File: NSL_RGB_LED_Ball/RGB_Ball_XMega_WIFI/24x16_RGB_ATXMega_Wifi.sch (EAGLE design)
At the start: 102 parts, among them IC2 TLC5947XLP, IC3 TLC5947XLP, IC4 TLC5947XLP, IC5 MCP73123, IC6 CC3000, IC7 MMA7455L, IC8 OPA344, X1 NX3225GA XC1972CT-ND

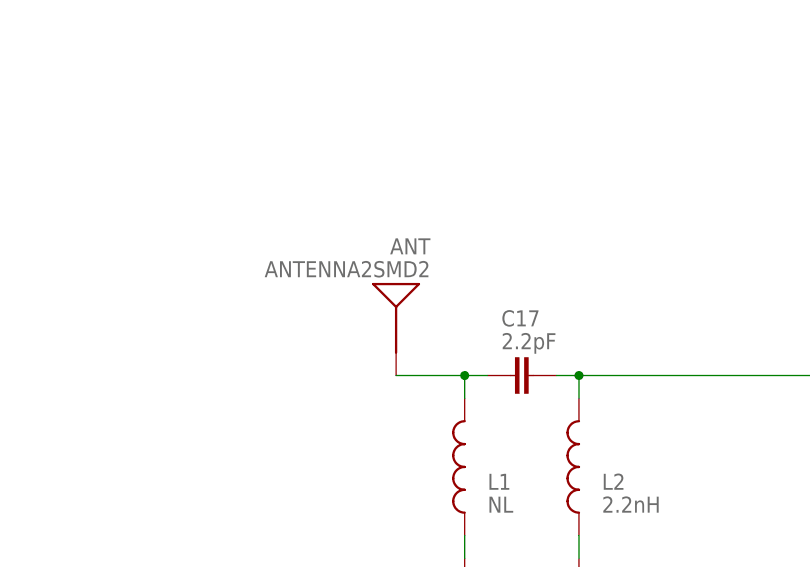
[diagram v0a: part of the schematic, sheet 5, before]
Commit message: 
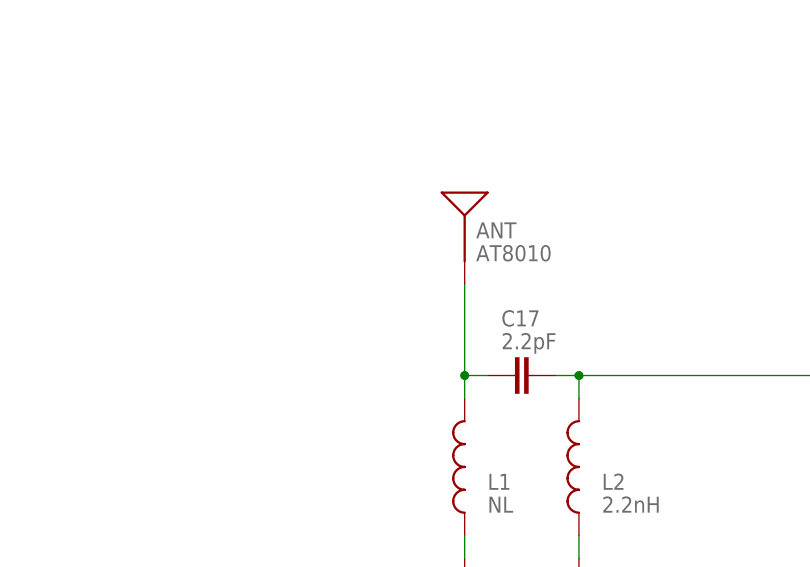
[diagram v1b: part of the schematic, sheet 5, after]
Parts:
- ANT: value ANTENNA2SMD2 -> AT8010; device SparkFun:ANTENNA2SMD2 -> 24x16_RGB_ATXMega_Wifi:ANTENNA2
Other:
- moved on the sheet: ANT
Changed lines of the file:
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@@
 <part name="SJ1" library="SparkFun" deviceset="SOLDERJUMPER" device="NO"/>
 <part name="SJ2" library="SparkFun" deviceset="SOLDERJUMPER" device="NO"/>
-<part name="ANT" library="SparkFun" deviceset="ANTENNA2" device="SMD2"/>
 <part name="U$1" library="8x8" deviceset="GND" device=""/>
 <part name="SJ3" library="SparkFun" deviceset="SOLDERJUMPER" device="NO"/>
+<part name="ANT" library="24x16_RGB_ATXMega_Wifi" deviceset="ANTENNA2" device="" value="AT8010"/>
 </parts>
 <sheets>
@@
 <instance part="SJ1" gate="1" x="-50.8" y="-27.94" rot="R90"/>
 <instance part="SJ2" gate="1" x="2.54" y="-55.88" rot="R180"/>
-<instance part="ANT" gate="G$1" x="-129.54" y="10.16" smashed="yes">
-<attribute name="NAME" x="-125.73" y="20.32" size="1.778" layer="95" rot="R180"/>
-<attribute name="VALUE" x="-125.73" y="17.78" size="1.778" layer="96" rot="R180"/>
-</instance>
 <instance part="SJ3" gate="1" x="-132.08" y="-81.28" rot="R90"/>
+<instance part="ANT" gate="G$1" x="-121.92" y="20.32"/>
 </instances>
 <busses>
@@
 <wire x1="-119.38" y1="5.08" x2="-121.92" y2="5.08" width="0.1524" layer="91"/>
 <wire x1="-121.92" y1="5.08" x2="-121.92" y2="2.54" width="0.1524" layer="91"/>
-<wire x1="-129.54" y1="5.08" x2="-121.92" y2="5.08" width="0.1524" layer="91"/>
+<wire x1="-121.92" y1="15.24" x2="-121.92" y2="5.08" width="0.1524" layer="91"/>
 <junction x="-121.92" y="5.08"/>
 <pinref part="ANT" gate="G$1" pin="SIGNAL"/>

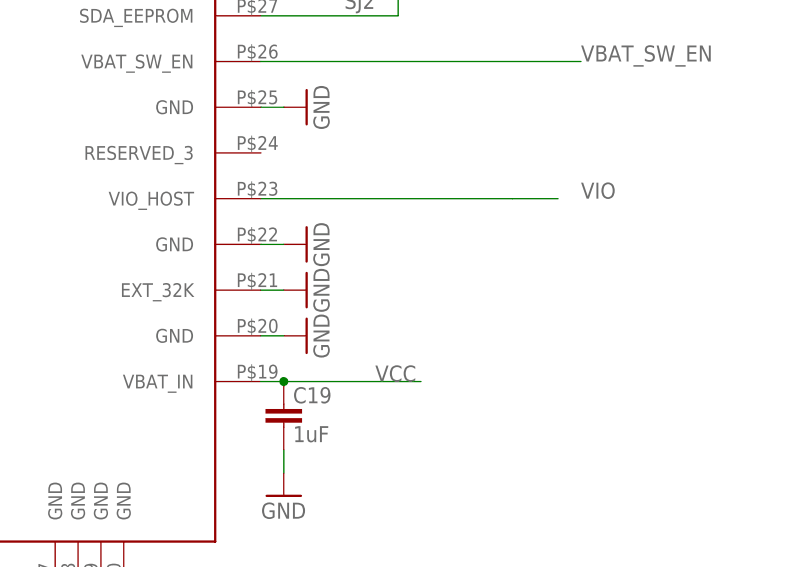
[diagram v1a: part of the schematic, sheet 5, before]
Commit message: 
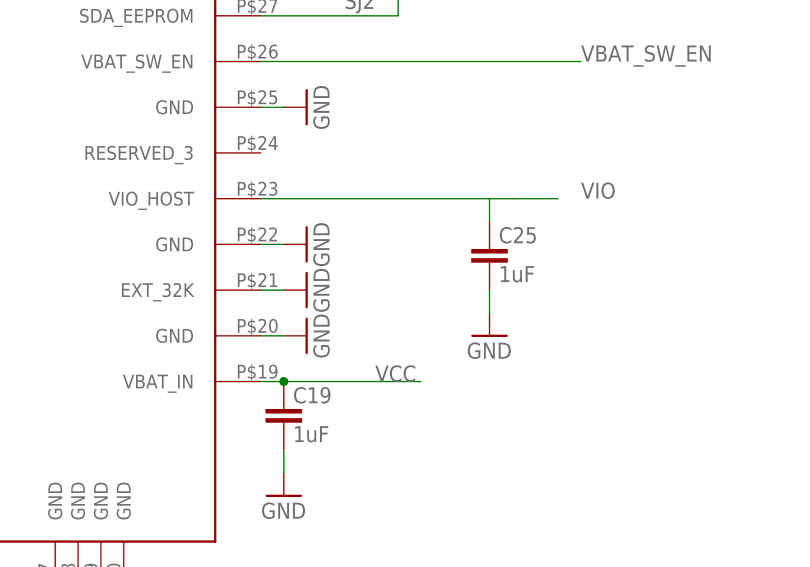
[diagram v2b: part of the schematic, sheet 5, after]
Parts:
- added C25: 1uF, SparkFun:CAP0805
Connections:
- net GND: now also C25.1
- net VIO: now also C25.2
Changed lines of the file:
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@@
 <part name="SJ3" library="SparkFun" deviceset="SOLDERJUMPER" device="NO"/>
 <part name="ANT" library="24x16_RGB_ATXMega_Wifi" deviceset="ANTENNA2" device="" value="AT8010"/>
+<part name="C25" library="SparkFun" deviceset="CAP" device="0805" value="1uF"/>
+<part name="GND19" library="supply1" deviceset="GND" device=""/>
 </parts>
 <sheets>
@@
 <instance part="SJ3" gate="1" x="-132.08" y="-81.28" rot="R90"/>
 <instance part="ANT" gate="G$1" x="-121.92" y="20.32"/>
+<instance part="C25" gate="G$1" x="17.78" y="-86.36" smashed="yes" rot="R180">
+<attribute name="NAME" x="18.796" y="-86.233" size="1.778" layer="95"/>
+<attribute name="VALUE" x="18.796" y="-90.551" size="1.778" layer="96"/>
+</instance>
+<instance part="GND19" gate="1" x="17.78" y="-96.52"/>
 </instances>
 <busses>
@@
 <wire x1="-109.22" y1="-15.24" x2="-109.22" y2="-12.7" width="0.1524" layer="91"/>
 </segment>
+<segment>
+<pinref part="C25" gate="G$1" pin="1"/>
+<pinref part="GND19" gate="1" pin="GND"/>
+<wire x1="17.78" y1="-91.44" x2="17.78" y2="-93.98" width="0.1524" layer="91"/>
+</segment>
 </net>
 <net name="VCC" class="0">
@@
 <segment>
 <pinref part="IC6" gate="G$1" pin="VIO_HOST"/>
-<wire x1="-7.62" y1="-81.28" x2="20.32" y2="-81.28" width="0.1524" layer="91"/>
+<wire x1="-7.62" y1="-81.28" x2="17.78" y2="-81.28" width="0.1524" layer="91"/>
+<wire x1="17.78" y1="-81.28" x2="20.32" y2="-81.28" width="0.1524" layer="91"/>
 <wire x1="20.32" y1="-81.28" x2="25.4" y2="-81.28" width="0.1524" layer="91"/>
 <label x="27.94" y="-81.28" size="1.778" layer="95"/>
-</segment>
-</net>
+<pinref part="C25" gate="G$1" pin="2"/>
+<wire x1="17.78" y1="-81.28" x2="17.78" y2="-83.82" width="0.1524" layer="91"/>
+</segment>
+</net>

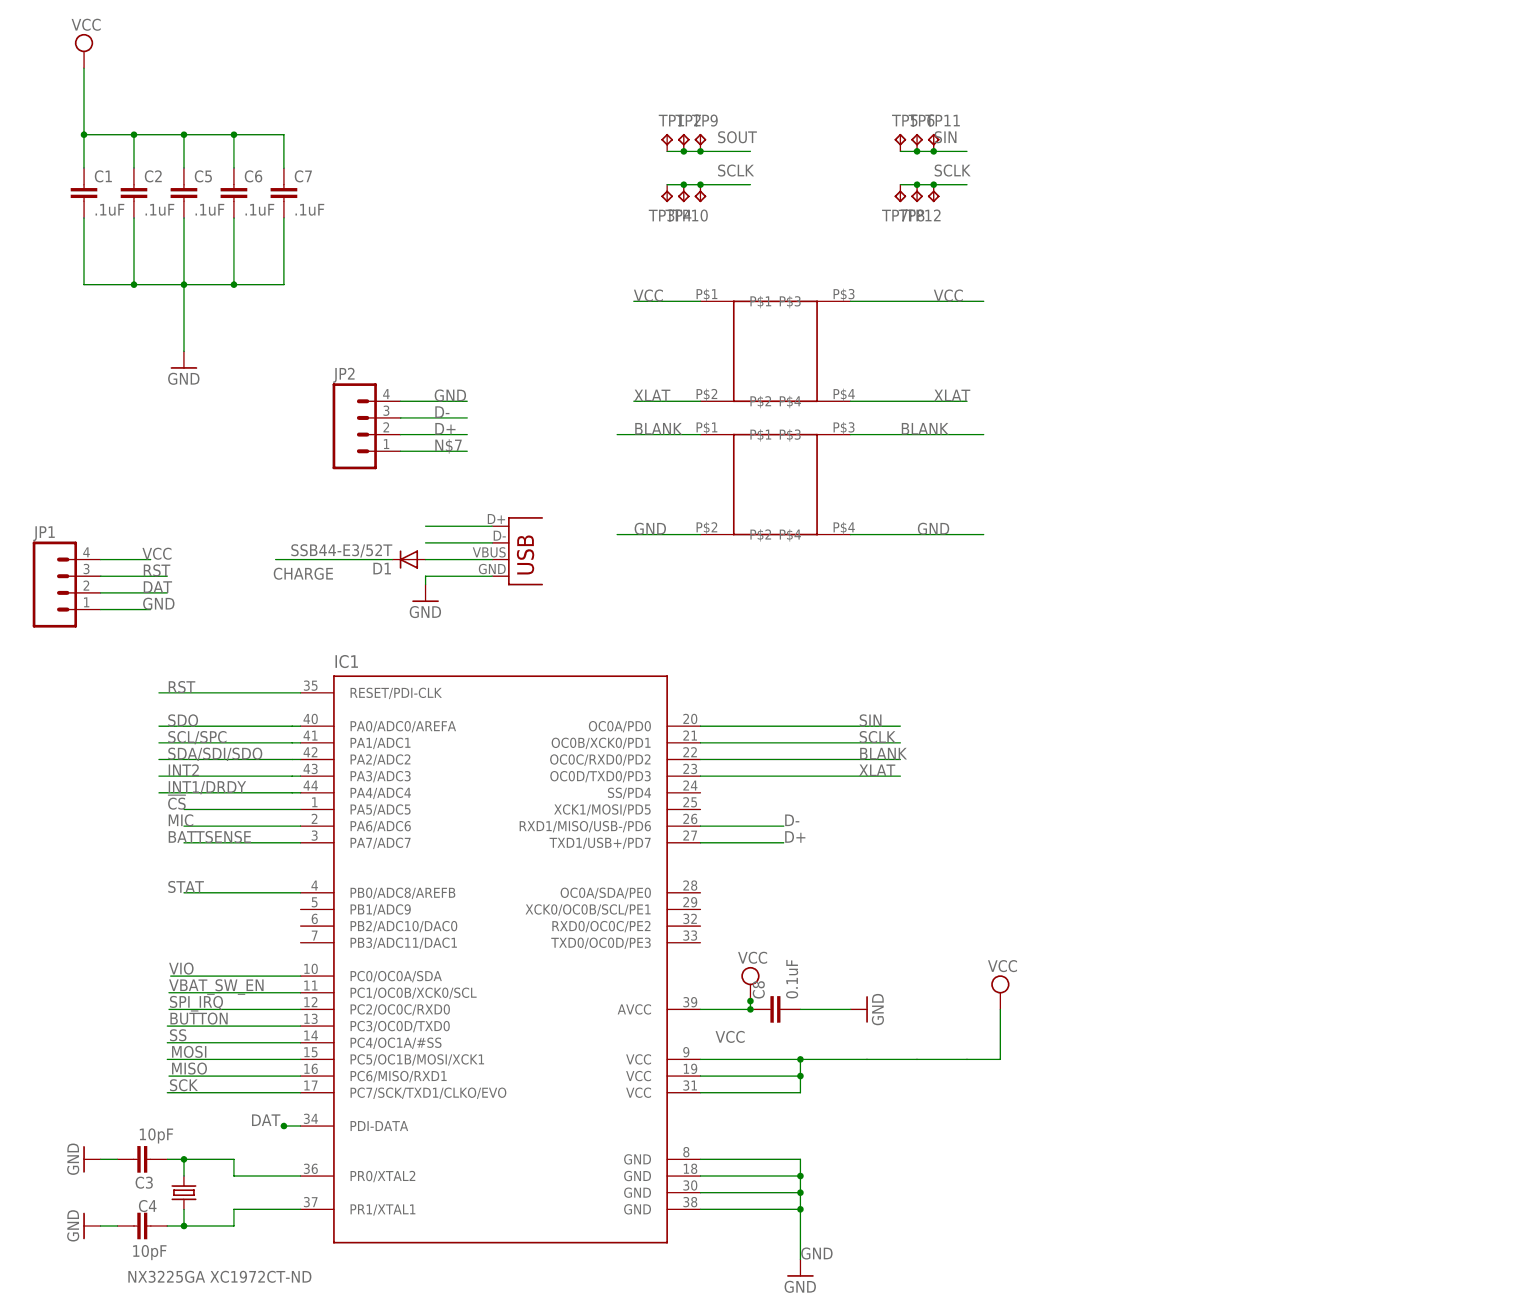
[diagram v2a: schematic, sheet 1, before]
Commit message: 
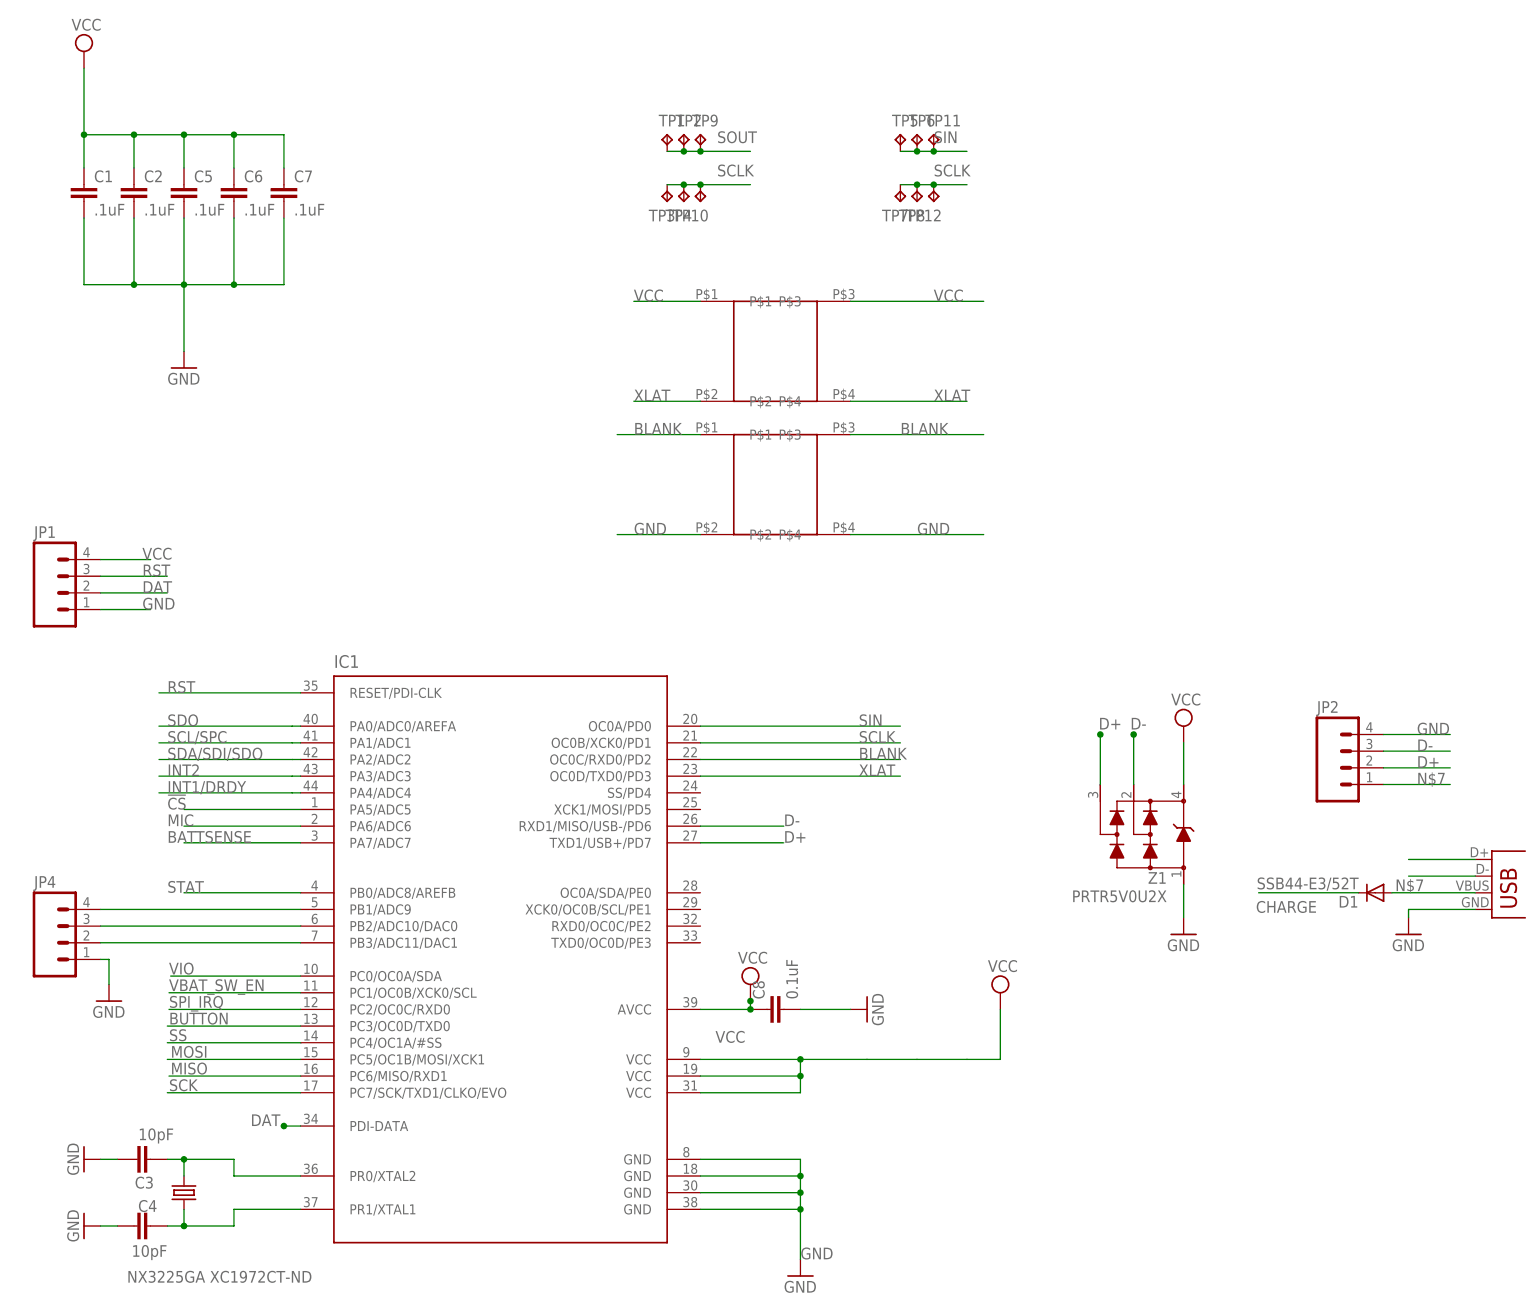
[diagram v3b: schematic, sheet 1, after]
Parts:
- added JP4: (no value), SparkFun-Connectors:M041.27MM
- added Z1: PRTR5V0U2X, USBug:PRTR5V0U2X
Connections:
- new net N$18: IC1.PB3/ADC11/DAC1, JP4.2
- new net N$4: IC1.PB1/ADC9, JP4.4
- new net N$5: IC1.PB2/ADC10/DAC0, JP4.3
- net D+: now also Z1.P$3
- net D-: now also Z1.P$2
- net GND: now also JP4.1, Z1.P$1
- net VCC: now also Z1.P$4
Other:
- moved on the sheet: D1, JP2
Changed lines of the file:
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@@
 <part name="C25" library="SparkFun" deviceset="CAP" device="0805" value="1uF"/>
 <part name="GND19" library="supply1" deviceset="GND" device=""/>
+<part name="JP4" library="SparkFun-Connectors" deviceset="M04" device="1.27MM"/>
+<part name="GND20" library="SparkFun" deviceset="GND" device=""/>
+<part name="Z1" library="USBug" deviceset="PRTR5V0U2X" device=""/>
+<part name="GND32" library="SparkFun" deviceset="GND" device=""/>
+<part name="SUPPLY4" library="supply2" deviceset="VCC" device=""/>
 </parts>
 <sheets>
@@
 <instance part="SUPPLY13" gate="G$1" x="27.94" y="-55.88"/>
 <instance part="JP1" gate="G$1" x="-76.2" y="3.81"/>
-<instance part="JP3" gate="G$1" x="-8.89" y="6.35"/>
-<instance part="GND12" gate="1" x="-21.59" y="2.54"/>
-<instance part="D1" gate="G$1" x="-24.13" y="8.89" rot="R180"/>
-<instance part="JP2" gate="G$1" x="-30.48" y="27.94"/>
+<instance part="JP3" gate="G$1" x="140.97" y="-44.45"/>
+<instance part="GND12" gate="1" x="128.27" y="-48.26"/>
+<instance part="D1" gate="G$1" x="123.19" y="-41.91" rot="R180"/>
+<instance part="JP2" gate="G$1" x="119.38" y="-22.86"/>
+<instance part="JP4" gate="G$1" x="-76.2" y="-49.53"/>
+<instance part="GND20" gate="1" x="-69.85" y="-58.42"/>
+<instance part="Z1" gate="G$1" x="88.9" y="-33.02" rot="MR0"/>
+<instance part="GND32" gate="1" x="93.98" y="-48.26"/>
+<instance part="SUPPLY4" gate="G$1" x="93.98" y="-16.51"/>
 </instances>
 <busses>
@@
 </segment>
 <segment>
-<wire x1="-11.43" y1="6.35" x2="-21.59" y2="6.35" width="0.1524" layer="91"/>
+<wire x1="138.43" y1="-44.45" x2="128.27" y2="-44.45" width="0.1524" layer="91"/>
 <pinref part="GND12" gate="1" pin="GND"/>
-<wire x1="-21.59" y1="6.35" x2="-21.59" y2="5.08" width="0.1524" layer="91"/>
+<wire x1="128.27" y1="-44.45" x2="128.27" y2="-45.72" width="0.1524" layer="91"/>
 <pinref part="JP3" gate="G$1" pin="GND"/>
 </segment>
 <segment>
-<wire x1="-15.24" y1="33.02" x2="-25.4" y2="33.02" width="0.1524" layer="91"/>
+<wire x1="134.62" y1="-17.78" x2="124.46" y2="-17.78" width="0.1524" layer="91"/>
 <pinref part="JP2" gate="G$1" pin="4"/>
-<label x="-20.32" y="33.02" size="1.778" layer="95"/>
+<label x="129.54" y="-17.78" size="1.778" layer="95"/>
+</segment>
+<segment>
+<pinref part="JP4" gate="G$1" pin="1"/>
+<pinref part="GND20" gate="1" pin="GND"/>
+<wire x1="-71.12" y1="-52.07" x2="-69.85" y2="-52.07" width="0.1524" layer="91"/>
+<wire x1="-69.85" y1="-52.07" x2="-69.85" y2="-55.88" width="0.1524" layer="91"/>
+</segment>
+<segment>
+<pinref part="Z1" gate="G$1" pin="P$1"/>
+<wire x1="93.98" y1="-40.64" x2="93.98" y2="-45.72" width="0.1524" layer="91"/>
+<pinref part="GND32" gate="1" pin="GND"/>
 </segment>
 </net>
@@
 <label x="-64.77" y="8.89" size="1.778" layer="95"/>
 </segment>
+<segment>
+<pinref part="Z1" gate="G$1" pin="P$4"/>
+<wire x1="93.98" y1="-25.4" x2="93.98" y2="-19.05" width="0.1524" layer="91"/>
+<pinref part="SUPPLY4" gate="G$1" pin="VCC"/>
+</segment>
 </net>
 <net name="RST" class="0">
@@
 </segment>
 <segment>
-<wire x1="-21.59" y1="11.43" x2="-11.43" y2="11.43" width="0.1524" layer="91"/>
+<wire x1="128.27" y1="-39.37" x2="138.43" y2="-39.37" width="0.1524" layer="91"/>
 <pinref part="JP3" gate="G$1" pin="D-"/>
 </segment>
 <segment>
-<wire x1="-25.4" y1="30.48" x2="-15.24" y2="30.48" width="0.1524" layer="91"/>
-<label x="-20.32" y="30.48" size="1.778" layer="95"/>
+<wire x1="124.46" y1="-20.32" x2="134.62" y2="-20.32" width="0.1524" layer="91"/>
+<label x="129.54" y="-20.32" size="1.778" layer="95"/>
 <pinref part="JP2" gate="G$1" pin="3"/>
+</segment>
+<segment>
+<pinref part="Z1" gate="G$1" pin="P$2"/>
+<wire x1="86.36" y1="-25.4" x2="86.36" y2="-17.78" width="0.1524" layer="91"/>
+<label x="85.852" y="-17.018" size="1.778" layer="95"/>
+<junction x="86.36" y="-17.78"/>
 </segment>
 </net>
@@
 </segment>
 <segment>
-<wire x1="-21.59" y1="13.97" x2="-11.43" y2="13.97" width="0.1524" layer="91"/>
+<wire x1="128.27" y1="-36.83" x2="138.43" y2="-36.83" width="0.1524" layer="91"/>
 <pinref part="JP3" gate="G$1" pin="D+"/>
 </segment>
 <segment>
-<wire x1="-25.4" y1="27.94" x2="-15.24" y2="27.94" width="0.1524" layer="91"/>
+<wire x1="124.46" y1="-22.86" x2="134.62" y2="-22.86" width="0.1524" layer="91"/>
 <pinref part="JP2" gate="G$1" pin="2"/>
-<label x="-20.32" y="27.94" size="1.778" layer="95"/>
+<label x="129.54" y="-22.86" size="1.778" layer="95"/>
+</segment>
+<segment>
+<pinref part="Z1" gate="G$1" pin="P$3"/>
+<wire x1="81.28" y1="-25.4" x2="81.28" y2="-17.78" width="0.1524" layer="91"/>
+<label x="81.026" y="-17.018" size="1.778" layer="95"/>
+<junction x="81.28" y="-17.78"/>
 </segment>
 </net>
@@
 <net name="CHARGE" class="0">
 <segment>
-<wire x1="-26.67" y1="8.89" x2="-44.45" y2="8.89" width="0.1524" layer="91"/>
+<wire x1="120.65" y1="-41.91" x2="105.41" y2="-41.91" width="0.1524" layer="91"/>
 <pinref part="D1" gate="G$1" pin="C"/>
-<label x="-35.56" y="7.62" size="1.778" layer="95" rot="R180"/>
+<label x="114.3" y="-43.18" size="1.778" layer="95" rot="R180"/>
 </segment>
 </net>
@@
 <pinref part="JP3" gate="G$1" pin="VBUS"/>
 <pinref part="D1" gate="G$1" pin="A"/>
-<wire x1="-11.43" y1="8.89" x2="-21.59" y2="8.89" width="0.1524" layer="91"/>
-</segment>
-<segment>
-<wire x1="-15.24" y1="25.4" x2="-25.4" y2="25.4" width="0.1524" layer="91"/>
+<wire x1="138.43" y1="-41.91" x2="125.73" y2="-41.91" width="0.1524" layer="91"/>
+<label x="126.238" y="-41.656" size="1.778" layer="95"/>
+</segment>
+<segment>
+<wire x1="134.62" y1="-25.4" x2="124.46" y2="-25.4" width="0.1524" layer="91"/>
 <pinref part="JP2" gate="G$1" pin="1"/>
-<label x="-20.32" y="25.4" size="1.778" layer="95"/>
+<label x="129.54" y="-25.4" size="1.778" layer="95"/>
 </segment>
 </net>
@@
 </segment>
 </net>
+<net name="N$4" class="0">
+<segment>
+<pinref part="IC1" gate="G$1" pin="PB1/ADC9"/>
+<wire x1="-40.64" y1="-44.45" x2="-71.12" y2="-44.45" width="0.1524" layer="91"/>
+<pinref part="JP4" gate="G$1" pin="4"/>
+</segment>
+</net>
+<net name="N$5" class="0">
+<segment>
+<pinref part="IC1" gate="G$1" pin="PB2/ADC10/DAC0"/>
+<wire x1="-40.64" y1="-46.99" x2="-71.12" y2="-46.99" width="0.1524" layer="91"/>
+<pinref part="JP4" gate="G$1" pin="3"/>
+</segment>
+</net>
+<net name="N$18" class="0">
+<segment>
+<pinref part="IC1" gate="G$1" pin="PB3/ADC11/DAC1"/>
+<wire x1="-40.64" y1="-49.53" x2="-71.12" y2="-49.53" width="0.1524" layer="91"/>
+<pinref part="JP4" gate="G$1" pin="2"/>
+</segment>
+</net>
